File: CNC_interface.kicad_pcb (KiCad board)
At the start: 2 copper layers, 31 parts, among them J1 Conn_01x04_Male, J10 Conn_01x08, J11 Conn_01x08, J12 Conn_01x08, J13 Conn_01x08, J14 Conn_01x03_Male, J15 Conn_01x03_Male, J16 Conn_01x03_Male, J17 Conn_01x08, J18 Conn_01x10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

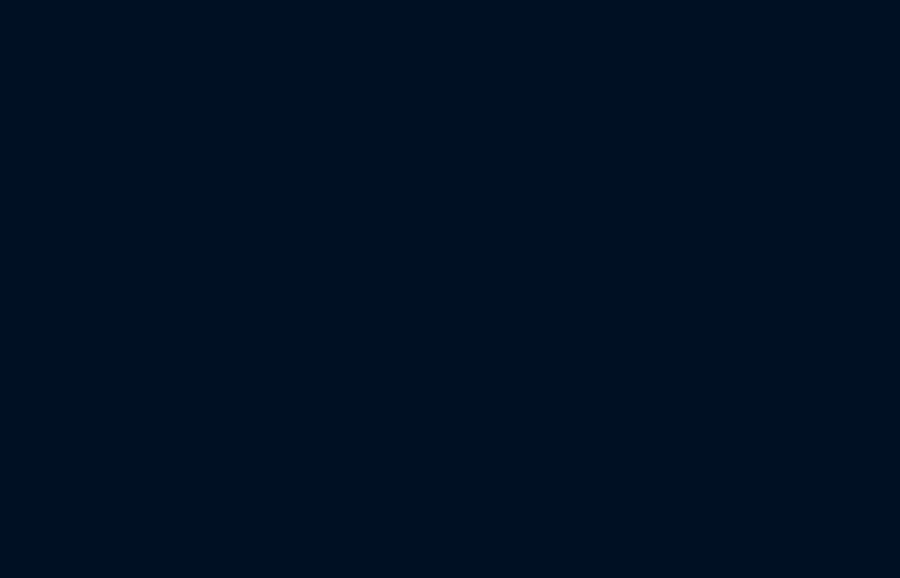
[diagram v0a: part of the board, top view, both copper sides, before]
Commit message: Changing 12 to 24V
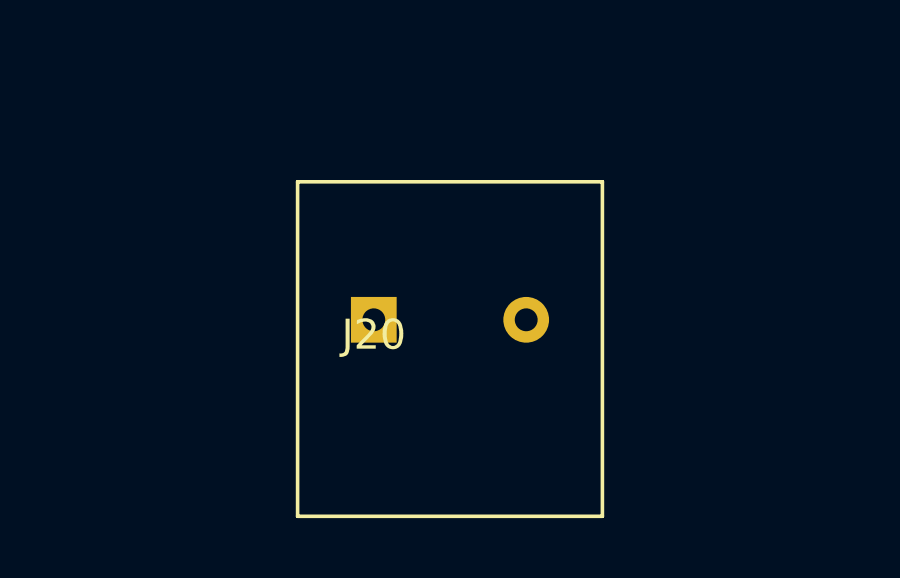
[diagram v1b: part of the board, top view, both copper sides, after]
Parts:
- added J20: Screw_Terminal_01x02, CNC_interface:TerminalBlock_Phoenix_MKDSP-1,5-2-5.08_1x02_P5.08mm, F.Cu at (132.1, 137.2)
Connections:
- J11 pad 7: unconnected-(J11-Pad7) -> +5V
- J13 pad 6: unconnected-(J13-Pad6) -> +5V
- J13 pad 7: unconnected-(J13-Pad7) -> +5V
- J9 pad 7: unconnected-(J9-Pad7) -> +5V

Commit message: add last footprints
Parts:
- added C3: 100uF, Capacitor_THT:CP_Radial_D6.3mm_P2.50mm, F.Cu at (88.9, 55.9)
- added C4: 100uF, Capacitor_THT:CP_Radial_D6.3mm_P2.50mm, F.Cu at (80.9, 55.9)
- added C5: 100uF, Capacitor_THT:CP_Radial_D6.3mm_P2.50mm, F.Cu at (96.9, 55.9)
- added R1: 100k, Resistor_THT:R_Axial_DIN0207_L6.3mm_D2.5mm_P10.16mm_Horizontal, F.Cu at (124.5, 109.2)
- added R2: 100k, Resistor_THT:R_Axial_DIN0207_L6.3mm_D2.5mm_P10.16mm_Horizontal, F.Cu at (124.5, 113.3)
- C1, C6: value CP -> 470uF; footprint Capacitor_THT:CP_Radial_D10.0mm_P5.00mm -> Capacitor_THT:CP_Radial_D12.5mm_P5.00mm
- C2, C7: value CP -> 220uF
- L1, L2, L3, L4: value L -> 10uH
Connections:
- J10 pad 8: +12V -> +24V
- J12 pad 8: +12V -> +24V
- J18 pad 1: 17 -> CONT
- J20 pad 2: CONTACT -> CONT
- J8 pad 8: +12V -> +24V

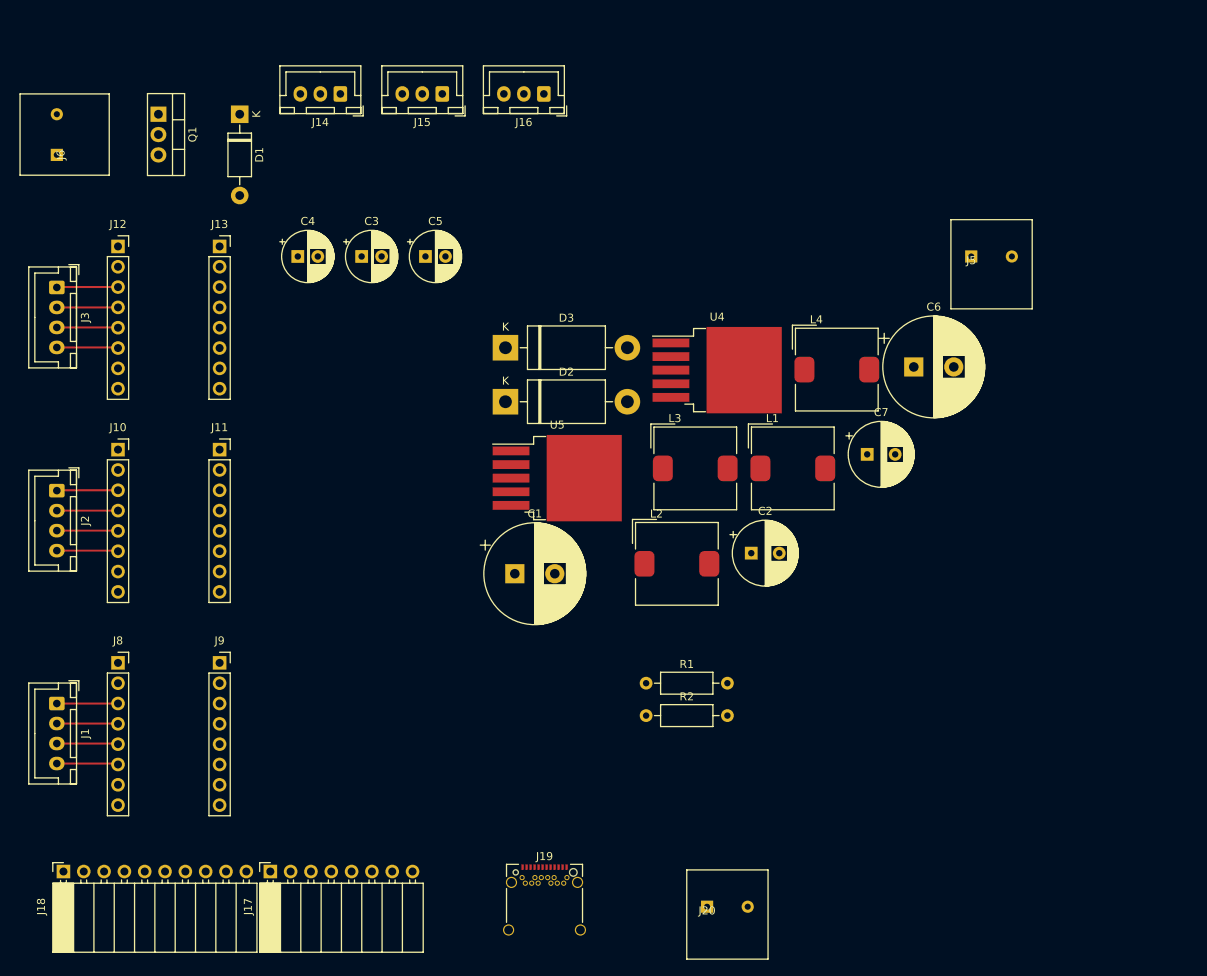
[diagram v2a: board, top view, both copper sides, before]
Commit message: update component names
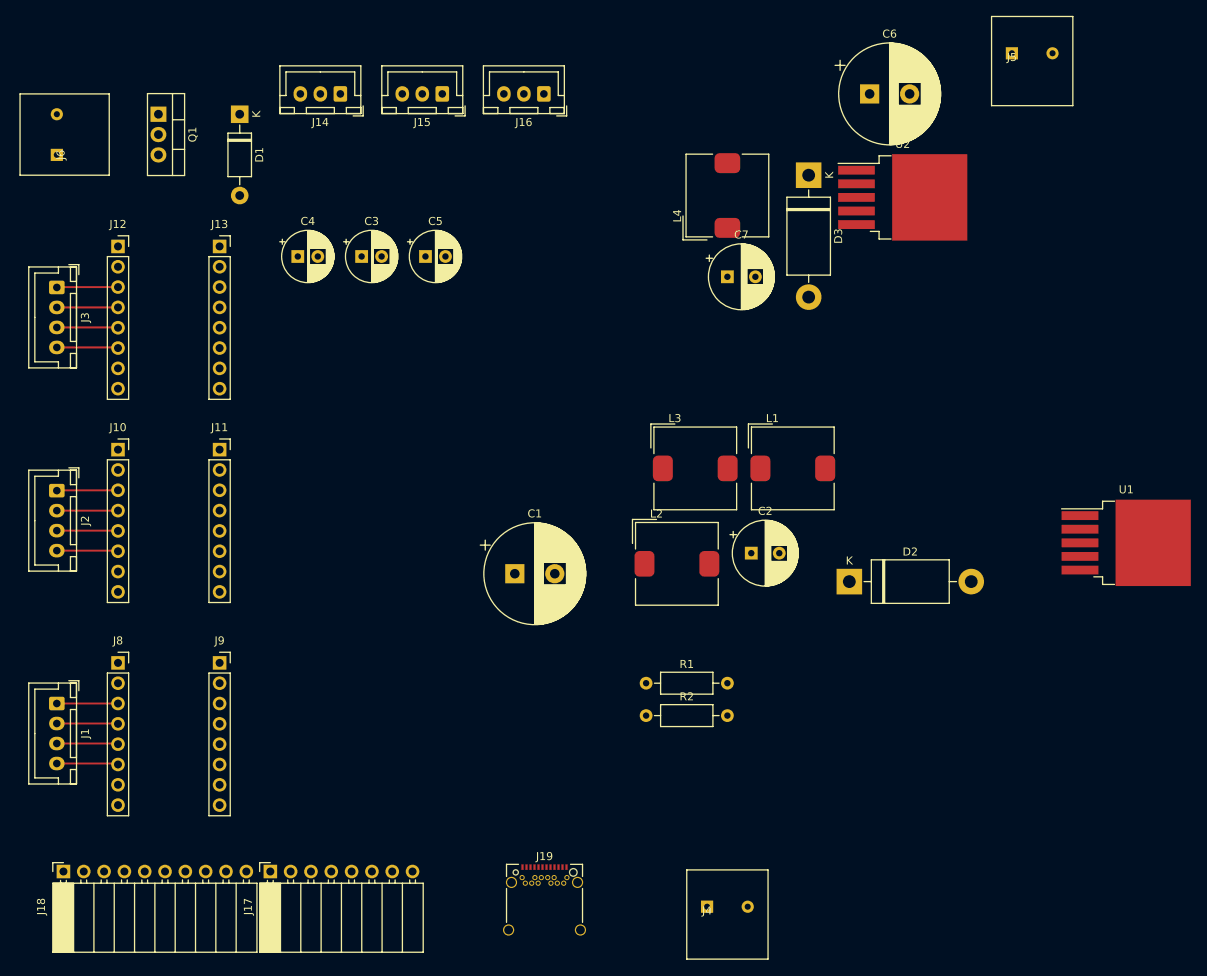
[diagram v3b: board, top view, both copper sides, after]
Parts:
- moved U2 55.6 mm to (156.5, 48.5)
- moved U1 55.5 mm to (184.5, 91.7)
- moved D2 48.5 mm to (149.9, 96.5)
- moved D3 43.6 mm to (144.8, 45.7), turned to -90 degrees
- moved C6 34.6 mm to (152.4, 35.6)
- moved C7 28.2 mm to (134.6, 58.4)
- moved J5 25.9 mm to (170.2, 30.5)
- moved L4 25.7 mm to (134.6, 48.3), turned to 90 degrees
- renumbered J20 to J4, U4 to U1, U5 to U2
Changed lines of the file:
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@@
   )
   (footprint "CNC_interface:TerminalBlock_Phoenix_MKDSP-1,5-2-5.08_1x02_P5.08mm" (layer "F.Cu")
-    (at 165.1 55.88)
+    (at 170.18 30.48)
     (property "Sheetfile" "CNC_interface.kicad_sch")
     (property "Sheetname" "")
@@
   )
   (footprint "Capacitor_THT:CP_Radial_D12.5mm_P5.00mm" (layer "F.Cu")
-    (at 157.914646 69.685)
+    (at 152.4 35.56)
     (descr "CP, Radial series, Radial, pin pitch=5.00mm, , diameter=12.5mm, Electrolytic Capacitor")
     (tags "CP Radial series Radial pin pitch 5.00mm  diameter 12.5mm Electrolytic Capacitor")
@@
   )
   (footprint "Capacitor_THT:CP_Radial_D8.0mm_P3.50mm" (layer "F.Cu")
-    (at 152.094698 80.615)
+    (at 134.62 58.42)
     (descr "CP, Radial series, Radial, pin pitch=3.50mm, , diameter=8mm, Electrolytic Capacitor")
     (tags "CP Radial series Radial pin pitch 3.50mm  diameter 8mm Electrolytic Capacitor")
@@
   )
   (footprint "Package_TO_SOT_SMD:TO-263-5_TabPin3" (layer "F.Cu")
-    (at 133.34 70.085)
+    (at 184.47 91.675)
     (descr "TO-263 / D2PAK / DDPAK SMD package, http://www.infineon.com/cms/en/product/packages/PG-TO263/PG-TO263-5-1/")
     (tags "D2PAK DDPAK TO-263 D2PAK-5 TO-263-5 SOT-426")
@@
     (property "Sheetname" "Power_stages")
     (attr smd)
-    (fp_text reference "U4" (at 0 -6.65) (layer "F.SilkS")
+    (fp_text reference "U1" (at 0 -6.65) (layer "F.SilkS")
       (effects (font (size 1 1) (thickness 0.15)))
     )
@@
   )
   (footprint "Diode_THT:D_DO-201AD_P15.24mm_Horizontal" (layer "F.Cu")
-    (at 106.88 74.035)
+    (at 149.86 96.52)
     (descr "Diode, DO-201AD series, Axial, Horizontal, pin pitch=15.24mm, , length*diameter=9.5*5.2mm^2, , http://www.diodes.com/_files/packages/DO-201AD.pdf")
     (tags "Diode DO-201AD series Axial Horizontal pin pitch 15.24mm  length 9.5mm diameter 5.2mm")
@@
   )
   (footprint "Diode_THT:D_DO-201AD_P15.24mm_Horizontal" (layer "F.Cu")
-    (at 106.88 67.285)
+    (at 144.78 45.72 -90)
     (descr "Diode, DO-201AD series, Axial, Horizontal, pin pitch=15.24mm, , length*diameter=9.5*5.2mm^2, , http://www.diodes.com/_files/packages/DO-201AD.pdf")
     (tags "Diode DO-201AD series Axial Horizontal pin pitch 15.24mm  length 9.5mm diameter 5.2mm")
@@
     (property "Sheetname" "Power_stages")
     (attr through_hole)
-    (fp_text reference "D3" (at 7.62 -3.72) (layer "F.SilkS")
-      (effects (font (size 1 1) (thickness 0.15)))
-    )
-    (fp_text value "D" (at 7.62 3.72) (layer "F.Fab")
-      (effects (font (size 1 1) (thickness 0.15)))
-    )
-    (fp_text user "K" (at 0 -2.6) (layer "F.SilkS")
-      (effects (font (size 1 1) (thickness 0.15)))
-    )
-    (fp_text user "K" (at 0 -2.6) (layer "F.Fab")
-      (effects (font (size 1 1) (thickness 0.15)))
-    )
-    (fp_text user "${REFERENCE}" (at 8.3325 0) (layer "F.Fab")
+    (fp_text reference "D3" (at 7.62 -3.72 90) (layer "F.SilkS")
+      (effects (font (size 1 1) (thickness 0.15)))
+    )
+    (fp_text value "D" (at 7.62 3.72 90) (layer "F.Fab")
+      (effects (font (size 1 1) (thickness 0.15)))
+    )
+    (fp_text user "K" (at 0 -2.6 90) (layer "F.SilkS")
+      (effects (font (size 1 1) (thickness 0.15)))
+    )
+    (fp_text user "K" (at 0 -2.6 90) (layer "F.Fab")
+      (effects (font (size 1 1) (thickness 0.15)))
+    )
+    (fp_text user "${REFERENCE}" (at 8.3325 0 90) (layer "F.Fab")
       (effects (font (size 1 1) (thickness 0.15)))
     )
@@
     (fp_line (start 4.295 -2.6) (end 4.295 2.6) (layer "F.Fab") (width 0.1))
     (fp_line (start 0 0) (end 2.87 0) (layer "F.Fab") (width 0.1))
-    (pad "1" thru_hole rect (at 0 0) (size 3.2 3.2) (drill 1.6) (layers *.Cu *.Mask)
+    (pad "1" thru_hole rect (at 0 0 270) (size 3.2 3.2) (drill 1.6) (layers *.Cu *.Mask)
       (net 9 "Net-(D3-Pad1)") (pinfunction "K") (pintype "passive"))
-    (pad "2" thru_hole oval (at 15.24 0) (size 3.2 3.2) (drill 1.6) (layers *.Cu *.Mask)
+    (pad "2" thru_hole oval (at 15.24 0 270) (size 3.2 3.2) (drill 1.6) (layers *.Cu *.Mask)
       (net 19 "GND") (pinfunction "A") (pintype "passive"))
     (model "${KICAD6_3DMODEL_DIR}/Diode_THT.3dshapes/D_DO-201AD_P15.24mm_Horizontal.wrl"
@@
   )
   (footprint "Inductor_SMD:L_TDK_SLF10145" (layer "F.Cu")
-    (at 148.295 70.02)
+    (at 134.62 48.26 90)
     (descr "Inductor, TDK, SLF10145, 10.1mmx10.1mm (Script generated with StandardBox.py) (https://product.tdk.com/info/en/catalog/datasheets/inductor_automotive_power_slf10145-h_en.pdf)")
     (tags "Inductor TDK_SLF10145")
@@
     (property "Sheetname" "Power_stages")
     (attr smd)
-    (fp_text reference "L4" (at -2.55 -6.25) (layer "F.SilkS")
-      (effects (font (size 1 1) (thickness 0.15)))
-    )
-    (fp_text value "10uH" (at 0 6.05) (layer "F.Fab")
-      (effects (font (size 1 1) (thickness 0.15)))
-    )
-    (fp_text user "" (at -49 0.05) (layer "F.SilkS")
+    (fp_text reference "L4" (at -2.55 -6.25 90) (layer "F.SilkS")
+      (effects (font (size 1 1) (thickness 0.15)))
+    )
+    (fp_text value "10uH" (at 0 6.05 90) (layer "F.Fab")
+      (effects (font (size 1 1) (thickness 0.15)))
+    )
+    (fp_text user "" (at -49 0.05 90) (layer "F.SilkS")
       (effects (font (size 3 3) (thickness 0.15)))
     )
-    (fp_text user "${REFERENCE}" (at 0 0) (layer "F.Fab")
+    (fp_text user "${REFERENCE}" (at 0 0 90) (layer "F.Fab")
       (effects (font (size 1 1) (thickness 0.15)))
     )
@@
     (fp_line (start 5.05 5.05) (end -5.05 5.05) (layer "F.Fab") (width 0.1))
     (fp_line (start -4.55 -5.05) (end 5.05 -5.05) (layer "F.Fab") (width 0.1))
-    (pad "1" smd roundrect (at -4.05 0) (size 2.5 3.2) (layers "F.Cu" "F.Paste" "F.Mask") (roundrect_rratio 0.25)
+    (pad "1" smd roundrect (at -4.05 0 90) (size 2.5 3.2) (layers "F.Cu" "F.Paste" "F.Mask") (roundrect_rratio 0.25)
       (net 63 "+12V") (pinfunction "1") (pintype "passive"))
-    (pad "2" smd roundrect (at 4.05 0) (size 2.5 3.2) (layers "F.Cu" "F.Paste" "F.Mask") (roundrect_rratio 0.25)
+    (pad "2" smd roundrect (at 4.05 0 90) (size 2.5 3.2) (layers "F.Cu" "F.Paste" "F.Mask") (roundrect_rratio 0.25)
       (net 9 "Net-(D3-Pad1)") (pinfunction "2") (pintype "passive"))
     (model "${KICAD6_3DMODEL_DIR}/Inductor_SMD.3dshapes/L_TDK_SLF10145.wrl"
@@
   )
   (footprint "Package_TO_SOT_SMD:TO-263-5_TabPin3" (layer "F.Cu")
-    (at 113.35 83.585)
+    (at 156.53 48.495)
     (descr "TO-263 / D2PAK / DDPAK SMD package, http://www.infineon.com/cms/en/product/packages/PG-TO263/PG-TO263-5-1/")
     (tags "D2PAK DDPAK TO-263 D2PAK-5 TO-263-5 SOT-426")
@@
     (property "Sheetname" "Power_stages")
     (attr smd)
-    (fp_text reference "U5" (at 0 -6.65) (layer "F.SilkS")
+    (fp_text reference "U2" (at 0 -6.65) (layer "F.SilkS")
       (effects (font (size 1 1) (thickness 0.15)))
     )
@@
     (property "Sheetname" "")
     (attr through_hole)
-    (fp_text reference "J20" (at 0 0.5) (layer "F.SilkS")
-      (effects (font (size 1 1) (thickness 0.15)))
-    )
+    (fp_text reference "J4" (at 0 0.5) (layer "F.SilkS")
+      (effects (font (size 1 1) (thickness 0.15)))
+    )

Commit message: place components on pcb
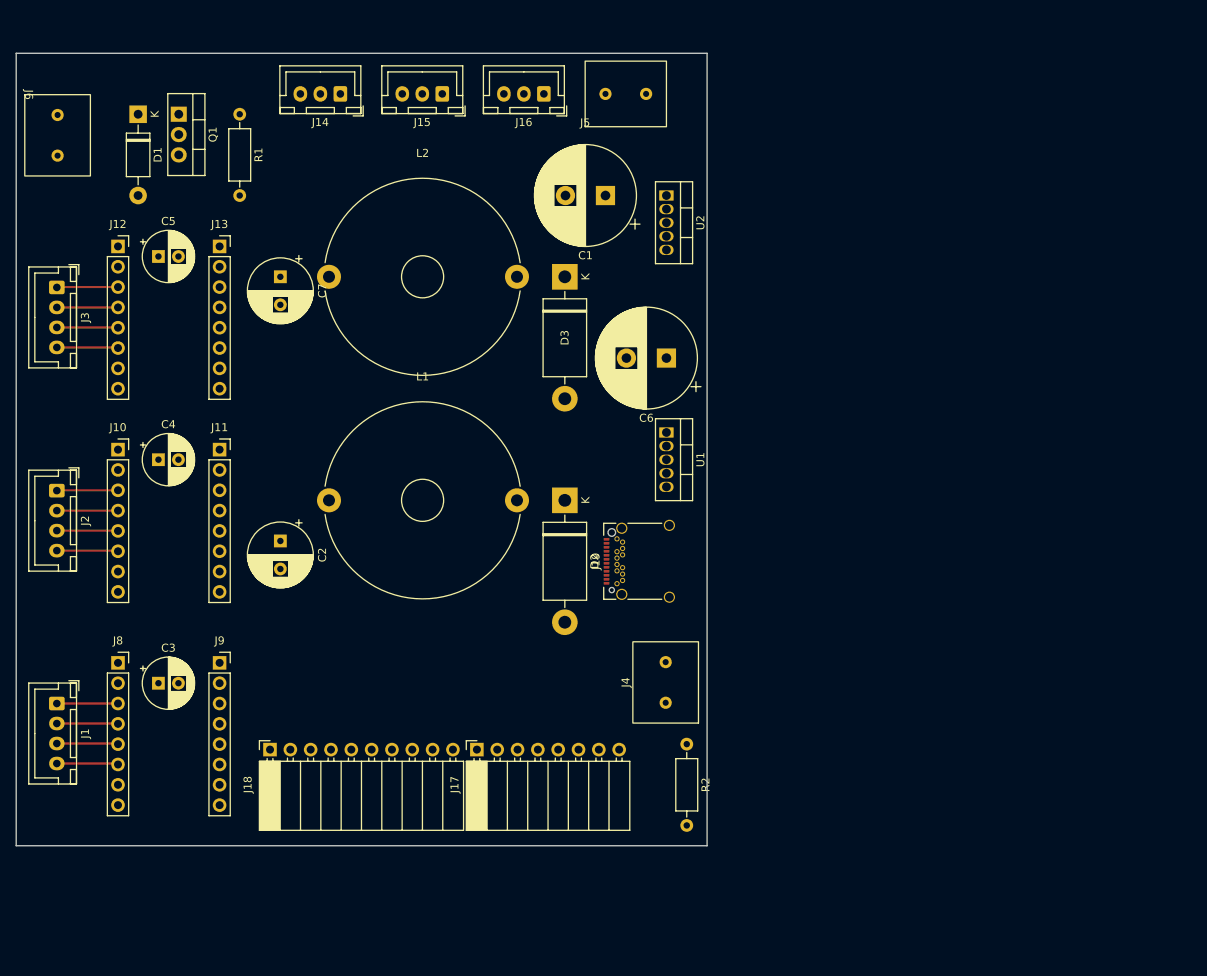
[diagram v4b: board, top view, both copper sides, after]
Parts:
- removed L3, L4: 10uH, Inductor_SMD:L_TDK_SLF10145
- C1, C6: value 470uF -> 100µF
- C2: value 220uF -> 1000uF
- C7: value 220uF -> 1000µF
- D2, D3: value D -> 1N5822
- J4, J5, J6: footprint CNC_interface:TerminalBlock_Phoenix_MKDSP-1,5-2-5.08_1x02_P5.08mm -> CNC_interface:RS_pro_screw_terminal_P5.08_x2
- L1: value 10uH -> 150µF; footprint Inductor_SMD:L_TDK_SLF10145 -> CNC_interface:L_Radial_24.4mm_P23.50mm_Murata_1400series
- L2: value 10uH -> 220µH; footprint Inductor_SMD:L_TDK_SLF10145 -> CNC_interface:L_Radial_24.4mm_P23.50mm_Murata_1400series
- U1: value LM2596S-5 -> LM2576HVT-5; footprint Package_TO_SOT_SMD:TO-263-5_TabPin3 -> Package_TO_SOT_THT:TO-220-5_Vertical
- U2: value LM2596S-12 -> LM2576HVT-12; footprint Package_TO_SOT_SMD:TO-263-5_TabPin3 -> Package_TO_SOT_THT:TO-220-5_Vertical
- moved R1 87.4 mm to (73.7, 38.1), turned to -90 degrees
- moved U1 59.1 mm to (127.0, 77.9), turned to -90 degrees
- moved C3 59.1 mm to (63.5, 109.2)
- moved C2 58.9 mm to (78.7, 91.4), turned to -90 degrees
- moved L1 58.1 mm to (84.8, 86.2)
- moved L2 56.5 mm to (84.8, 58.2)
- moved C7 55.9 mm to (78.7, 58.4), turned to -90 degrees
- moved J5 54.1 mm to (116.8, 39.7)
- moved C1 48.6 mm to (119.4, 48.3), turned to 180 degrees
- moved J19 45.1 mm to (124.5, 94.0), turned to 90 degrees
- moved C6 41.7 mm to (127.0, 68.6), turned to 180 degrees
- moved D2 37.0 mm to (114.3, 86.4), turned to -90 degrees
- moved C5 33.4 mm to (63.5, 55.9)
- moved D3 33.0 mm to (114.3, 58.4)
- moved C4 30.8 mm to (63.5, 81.3)
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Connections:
- L1 pad 1: Net-(L1-Pad1) -> +5V
- L2 pad 1: Net-(L2-Pad1) -> +12V
- L2 pad 2: Net-(L1-Pad1) -> Net-(D3-Pad1)
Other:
- board outline added: 86.4 x 99.1 mm
